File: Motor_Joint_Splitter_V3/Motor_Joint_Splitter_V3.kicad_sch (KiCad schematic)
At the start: 24 parts, among them J1 Conn_01x05, J2 26605030, J3 Conn_01x03_Socket, J7 ethernet_54602-908LF, J9 Conn_01x05, U2 74ACT244MTCX

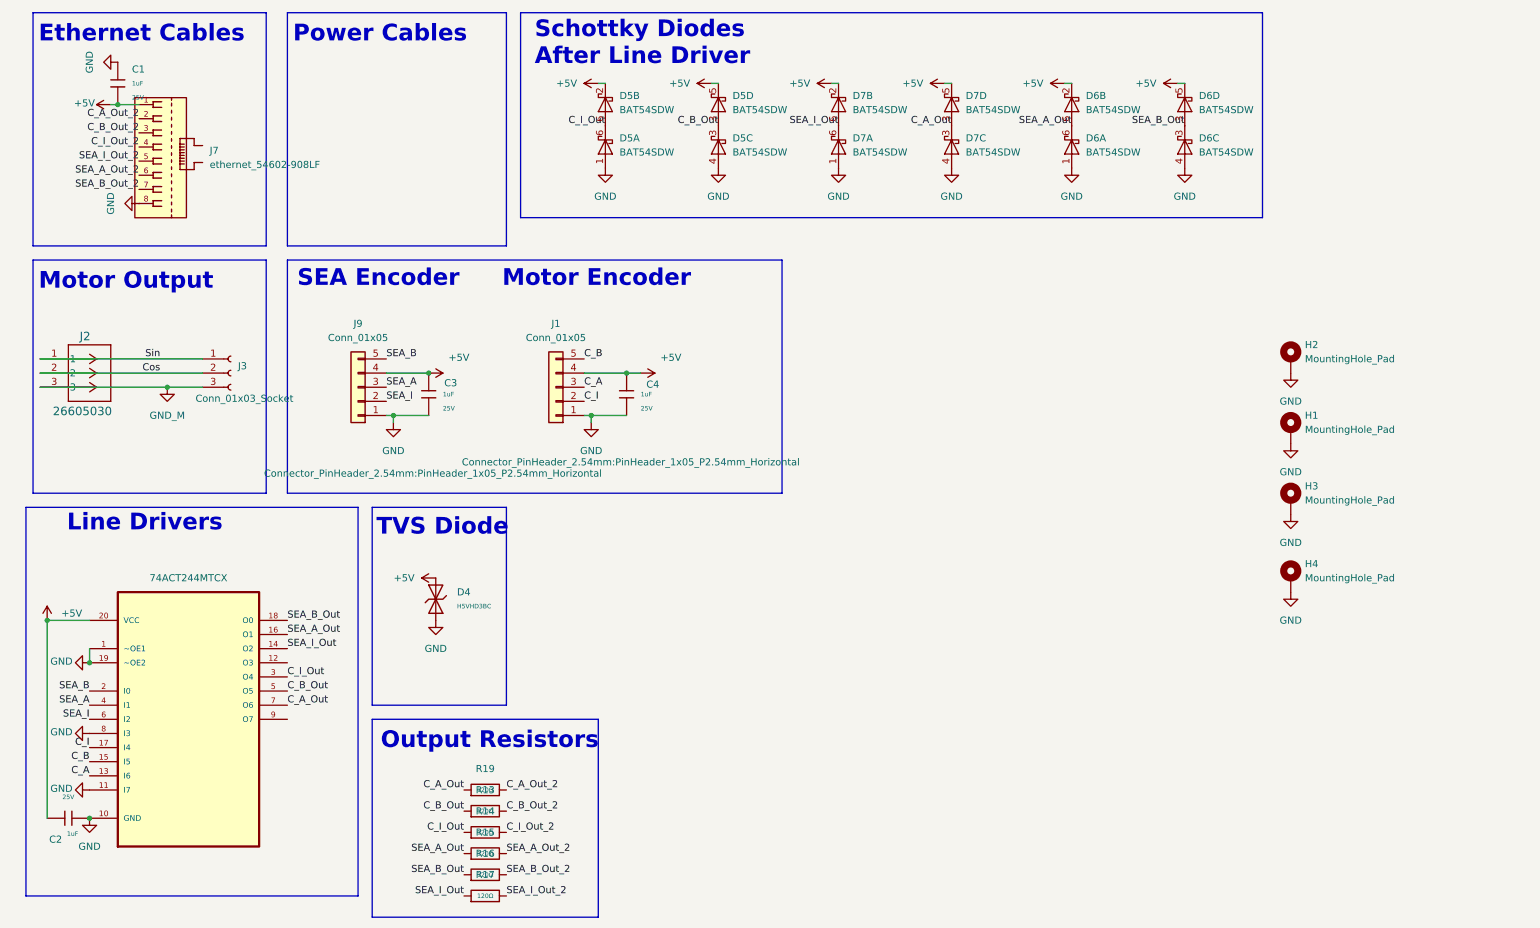
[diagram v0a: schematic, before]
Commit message: Finished updating the joint splitter design. May want to consider using rows of single buffers rather than the octal buffer to prevent crosstalk.
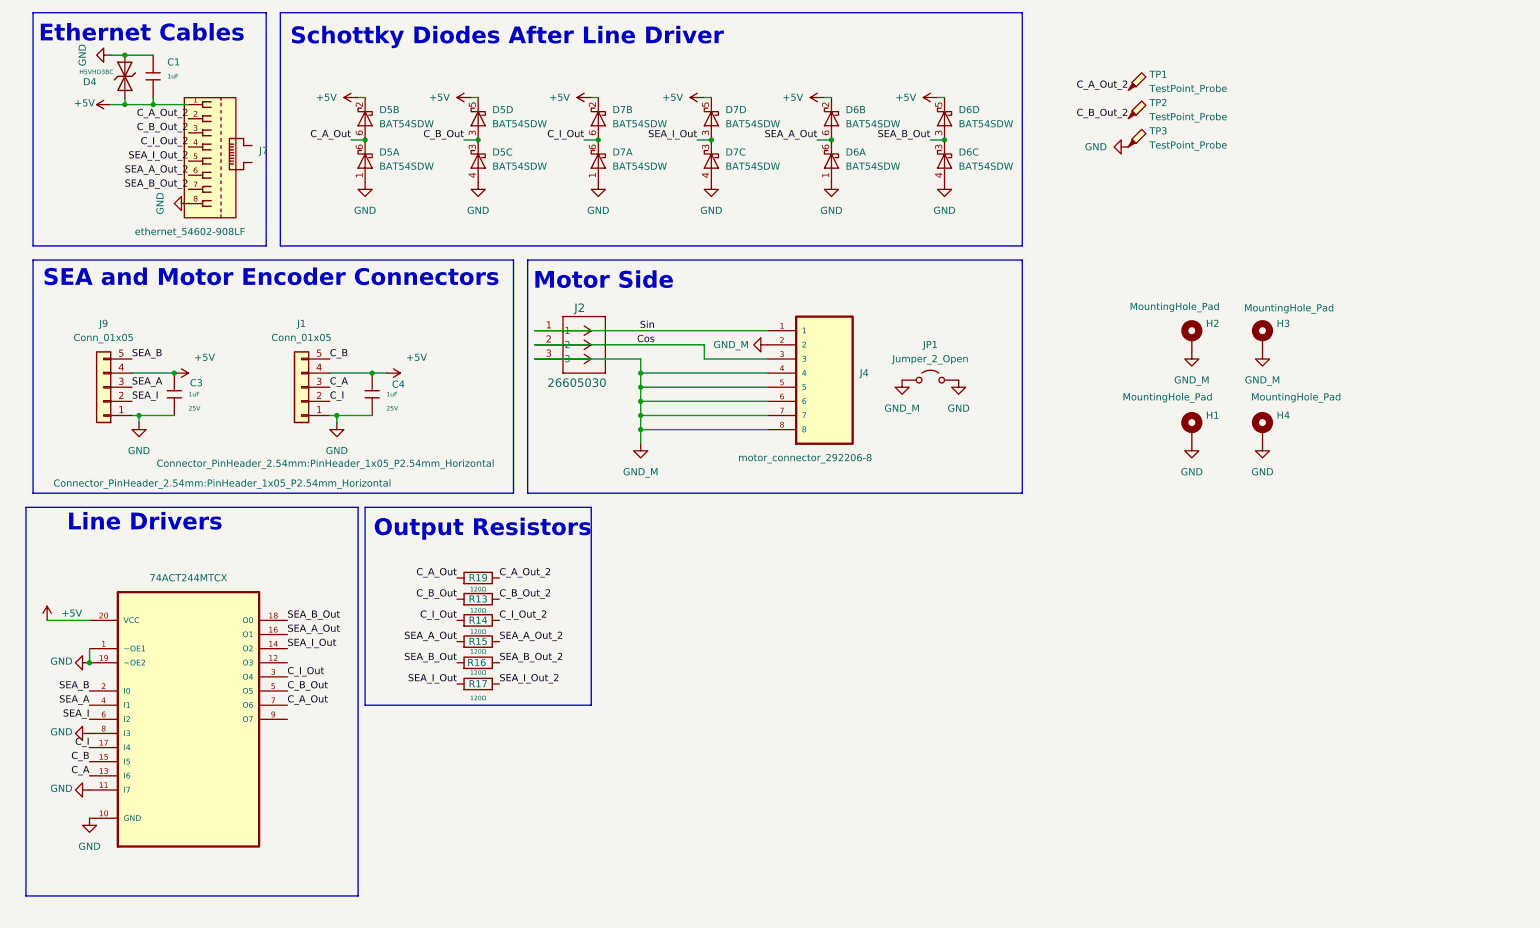
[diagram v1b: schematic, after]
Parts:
- removed C2: 1uF, PCM_JLCPCB:C_0402, symbol PCM_JLCPCB-Capacitors:0402,1uF
- removed J3: Conn_01x03_Socket, symbol Connector:Conn_01x03_Socket
- added J4: motor_connector_292206-8, splitter_parts:TE_292206-8, symbol splitter_parts:motor_connector_292206-8
- added JP1: Jumper_2_Open, TestPoint:TestPoint_2Pads_Pitch5.08mm_Drill1.3mm, symbol Jumper:Jumper_2_Open
- added TP1, TP2, TP3: TestPoint_Probe, TestPoint:TestPoint_Bridge_Pitch2.54mm_Drill1.0mm, symbol Connector:TestPoint_Probe
- J1, J9: LCSC (none) -> C138801
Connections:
- net C_A_Out: now also D5.6 (A), D5.6 (K); no longer D7.3 (A), D7.3 (K)
- net C_A_Out_2: now also TP1.1
- net C_B_Out_2: now also TP2.1
- net C_I_Out: now also D7.6 (A), D7.6 (K); no longer D5.6 (A), D5.6 (K)
- net Cos: now also J4.3
- net GND: now also JP1.2 (B), TP3.1; no longer H2.1, H3.1
- net GND_M: now also H2.1, H3.1, J4.2, J4.4, J4.5, J4.6, J4.7, J4.8, JP1.1 (A)
- net SEA_I_Out: now also D7.3 (A), D7.3 (K); no longer D7.6 (A), D7.6 (K)
- net Sin: now also J4.1
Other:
- note added: "Motor Side"
- note added: "SEA and Motor Encoder Connectors"
- note removed: "Motor Encoder"
- note removed: "Motor Output"
- note removed: "Power Cables"
- note removed: "SEA Encoder"
- note removed: "TVS Diode"
- moved on the sheet: C1, C3, C4, D4, D5A, D5B, D5C, D5D, D6A, D6B, D6C, D6D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

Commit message: Finished new version of the Motor Joint Splitter (v3). Includes separated grounding for power and signal, new encoder connectors, and PCBA compatible assembly for faster and cheaper orders.
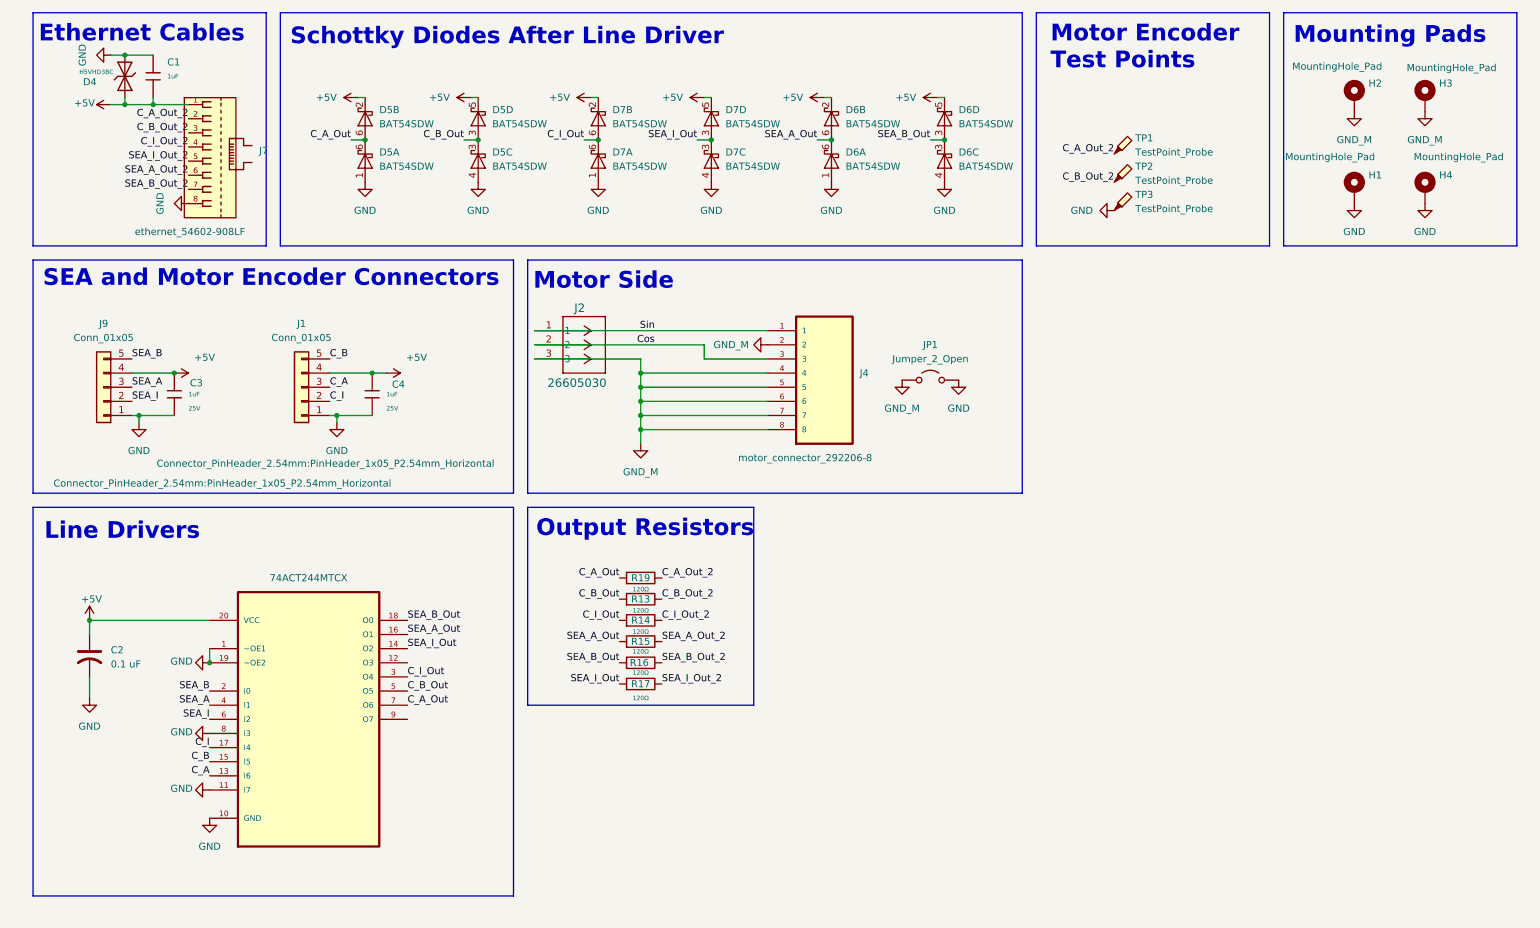
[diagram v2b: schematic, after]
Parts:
- added C2: 0.1 uF, PCM_JLCPCB:C_0603, symbol Device:C_US
- D5, D6, D7: footprint Package_TO_SOT_SMD:SOT-363_SC-70-6 -> PCM_JLCPCB:SOT-363_SC-70-6
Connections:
- net +5V: now also C2.1
- net GND: now also C2.2
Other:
- note added: "Motor Encoder Test Points"
- note added: "Mounting Pads"
- moved on the sheet: H1, H2, H3, H4, R13, R14, R15, R16, R17, R19, TP1, TP2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
